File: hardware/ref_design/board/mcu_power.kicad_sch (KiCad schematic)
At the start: 19 parts

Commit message: Reference design: board routed and DRC clean
- Core copy made faithful: Raspberry Pi's 0402 land patterns for the core
  passives (tools/lib_from_ref.py), their 3V3 stubs into the pour under the
  chip kept, and the uncopied-pad check made layer-aware (their board has a
  second flash footprint on the back, which had cost every QSPI track).
- TPS63001 re-placed and its power loop drawn by route.py as TI's layout
  guidance asks.
- tools/maze.py: a small A* router for the flash's SD2 line and for any
  connection Freerouting leaves open, with bounded rip-up.
- route.py: order-stable pre-routes (so --reuse is valid), fiducial
  keep-outs for the router, a second Freerouting pass when needed with a
  watchdog for its warning dialog, loose-copper cleanup.

check_pcb.py: 0 errors, 0 unconnected, 0 schematic parity issues.

Co-Authored-By: Claude Opus 5.5 (1M context) <noreply@anthropic.com>
Claude-Session: https://claude.ai/code/session_01KGgEu3CbFtCsvHRQgAFiCN
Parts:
- C10, C11, C12, C13, C14, C15, C16, C17, C18, C19, C20, C21, C22, C26: footprint Capacitor_SMD:C_0402_1005Metric -> battler:C_0402_1005Metric_RPi
- C24, C25: footprint Capacitor_SMD:C_0402_1005Metric -> battler:C_0402_1005Metric_RPi_Wide
- R19: footprint Resistor_SMD:R_0402_1005Metric -> battler:R_0402_1005Metric_RPi
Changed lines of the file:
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@@
         (font
           (size 1.27 1.27))))
-    (property "Footprint" "Capacitor_SMD:C_0402_1005Metric"
+    (property "Footprint" "battler:C_0402_1005Metric_RPi"
       (at 30.48 35.56 0)
       (effects
@@
         (font
           (size 1.27 1.27))))
-    (property "Footprint" "Capacitor_SMD:C_0402_1005Metric"
+    (property "Footprint" "battler:C_0402_1005Metric_RPi"
       (at 58.42 35.56 0)
       (effects
@@
         (font
           (size 1.27 1.27))))
-    (property "Footprint" "Capacitor_SMD:C_0402_1005Metric"
+    (property "Footprint" "battler:C_0402_1005Metric_RPi"
       (at 86.36 35.56 0)
       (effects
@@
         (font
           (size 1.27 1.27))))
-    (property "Footprint" "Capacitor_SMD:C_0402_1005Metric"
+    (property "Footprint" "battler:C_0402_1005Metric_RPi"
       (at 114.3 35.56 0)
       (effects
@@
         (font
           (size 1.27 1.27))))
-    (property "Footprint" "Capacitor_SMD:C_0402_1005Metric"
+    (property "Footprint" "battler:C_0402_1005Metric_RPi"
       (at 142.24 35.56 0)
       (effects
@@
         (font
           (size 1.27 1.27))))
-    (property "Footprint" "Capacitor_SMD:C_0402_1005Metric"
+    (property "Footprint" "battler:C_0402_1005Metric_RPi"
       (at 170.18 35.56 0)
       (effects
@@
         (font
           (size 1.27 1.27))))
-    (property "Footprint" "Capacitor_SMD:C_0402_1005Metric"
+    (property "Footprint" "battler:C_0402_1005Metric_RPi"
       (at 198.12 35.56 0)
       (effects
@@
         (font
           (size 1.27 1.27))))
-    (property "Footprint" "Capacitor_SMD:C_0402_1005Metric"
+    (property "Footprint" "battler:C_0402_1005Metric_RPi"
       (at 226.06 35.56 0)
       (effects
@@
         (font
           (size 1.27 1.27))))
-    (property "Footprint" "Capacitor_SMD:C_0402_1005Metric"
+    (property "Footprint" "battler:C_0402_1005Metric_RPi"
       (at 30.48 50.8 0)
       (effects
@@
         (font
           (size 1.27 1.27))))
-    (property "Footprint" "Capacitor_SMD:C_0402_1005Metric"
+    (property "Footprint" "battler:C_0402_1005Metric_RPi"
       (at 58.42 50.8 0)
       (effects
@@
         (font
           (size 1.27 1.27))))
-    (property "Footprint" "Capacitor_SMD:C_0402_1005Metric"
+    (property "Footprint" "battler:C_0402_1005Metric_RPi"
       (at 142.24 50.8 0)
       (effects
@@
         (font
           (size 1.27 1.27))))
-    (property "Footprint" "Capacitor_SMD:C_0402_1005Metric"
+    (property "Footprint" "battler:C_0402_1005Metric_RPi"
       (at 170.18 50.8 0)
       (effects
@@
         (font
           (size 1.27 1.27))))
-    (property "Footprint" "Capacitor_SMD:C_0402_1005Metric"
+    (property "Footprint" "battler:C_0402_1005Metric_RPi"
       (at 198.12 50.8 0)
       (effects
@@
         (font
           (size 1.27 1.27))))
-    (property "Footprint" "Capacitor_SMD:C_0402_1005Metric"
+    (property "Footprint" "battler:C_0402_1005Metric_RPi_Wide"
       (at 114.3 50.8 0)
       (effects
@@
         (font
           (size 1.27 1.27))))
-    (property "Footprint" "Capacitor_SMD:C_0402_1005Metric"
+    (property "Footprint" "battler:C_0402_1005Metric_RPi_Wide"
       (at 226.06 50.8 0)
       (effects
@@
         (font
           (size 1.27 1.27))))
-    (property "Footprint" "Capacitor_SMD:C_0402_1005Metric"
+    (property "Footprint" "battler:C_0402_1005Metric_RPi"
       (at 104.14 66.04 0)
       (effects
@@
         (font
           (size 1.27 1.27))))
-    (property "Footprint" "Resistor_SMD:R_0402_1005Metric"
+    (property "Footprint" "battler:R_0402_1005Metric_RPi"
       (at 66.04 66.04 0)
       (effects

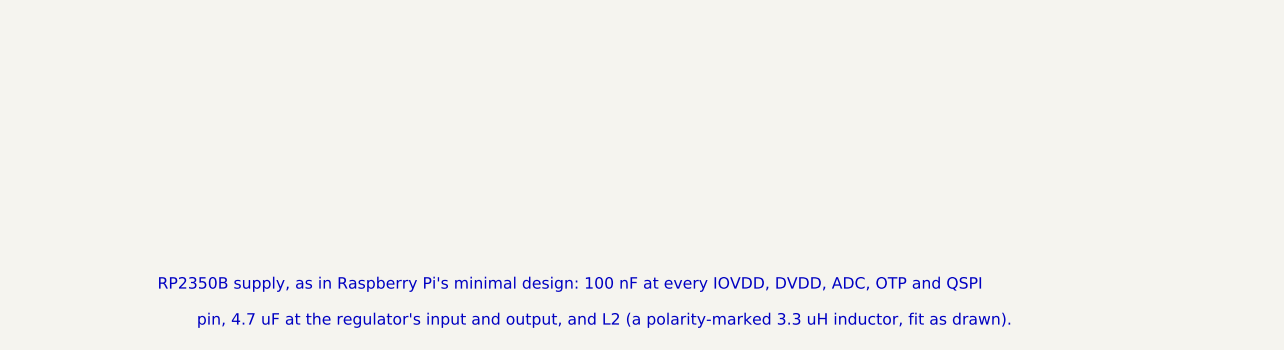
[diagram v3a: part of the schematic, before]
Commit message: 2-layer fork: approved circuit changes in the design data and schematic
TP4056 charger (500 mA, TEMP grounded) with USB load sharing (B5819W, AO3401A
gate fed through a BAT54WS so it switches at once on an unplug, 22 uF on VSYS),
ME6211 3V3 LDO on the power latch, RP2354B with its flash inside (only the
QSPI_SS strap outside), 27 ohm 0603 USB resistors, SRV05-4 ESD, PWM audio
through two RC poles into an FM8002A, seat 1's Y contact as the power button,
no LEDs, no thermistor. Thermal-via footprints use 0.3 mm holes. Netlist
check passes, ERC 0 errors.

Co-Authored-By: Claude Opus 5.5 <noreply@anthropic.com>
Claude-Session: https://claude.ai/code/session_01KGgEu3CbFtCsvHRQgAFiCN
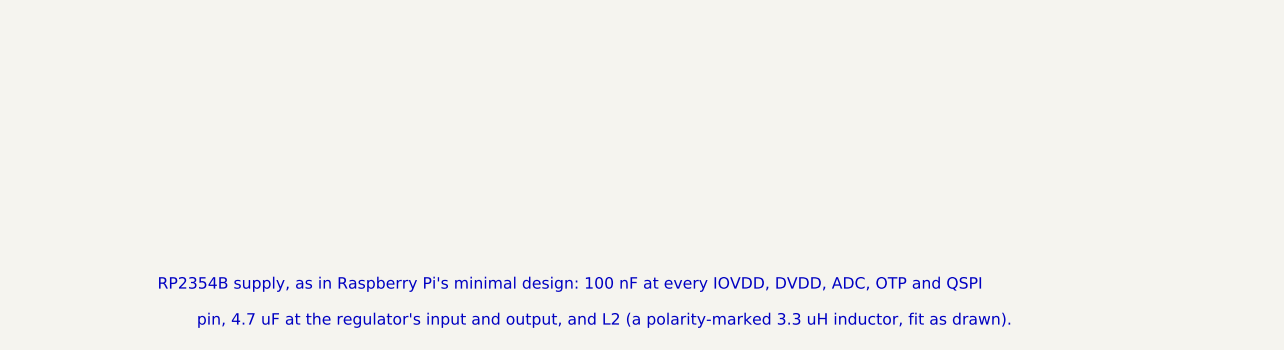
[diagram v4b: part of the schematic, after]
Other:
- note added: "RP2354B supply, as in Raspberry Pi's minimal design: 100 nF at every IOVDD, DVDD, ADC, OTP and QSPI"
- note removed: "RP2350B supply, as in Raspberry Pi's minimal design: 100 nF at every IOVDD, DVDD, ADC, OTP and QSPI"
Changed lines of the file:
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@@
       (xy 266.7 50.8))
 )
-  (text "RP2350B supply, as in Raspberry Pi's minimal design: 100 nF at every IOVDD, DVDD, ADC, OTP and QSPI"
+  (text "RP2354B supply, as in Raspberry Pi's minimal design: 100 nF at every IOVDD, DVDD, ADC, OTP and QSPI"
     (at 63.5 180 0)
     (effects
